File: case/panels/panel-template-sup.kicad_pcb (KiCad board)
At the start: 2 copper layers, 100 x 190 mm, 4 parts

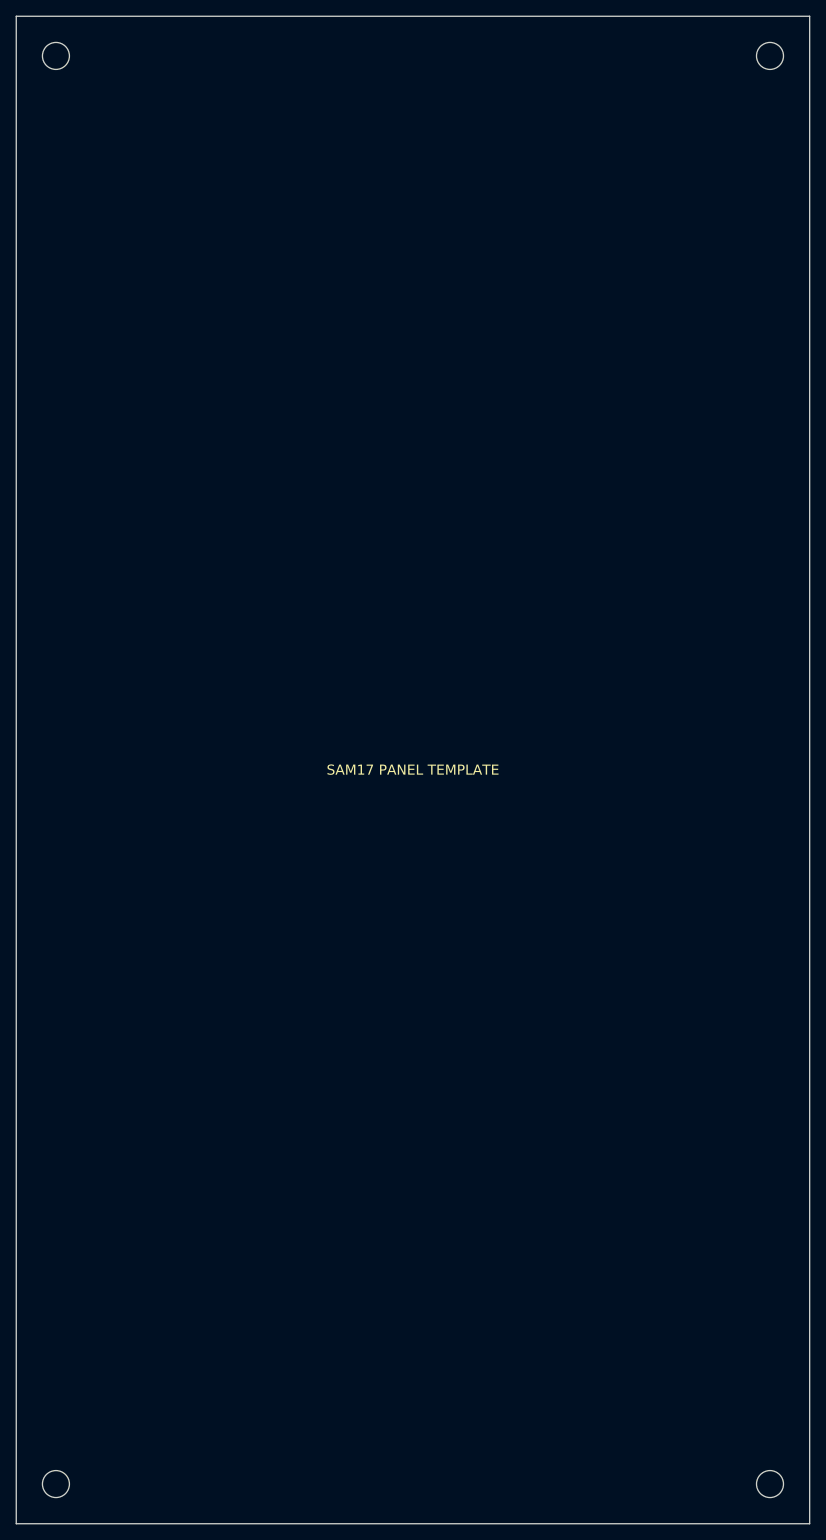
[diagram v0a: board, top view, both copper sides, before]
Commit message: Case: la silueta pasa a triangulo modernista, y tres fallos de raiz que salieron por el camino
La silueta del costado se rehizo entera sobre renders sucesivos. Deja de ser
una bota escalonada y pasa a ser un triangulo rectangulo con la hipotenusa
quebrada en dos tramos y el valle en medio:

  ancho 500   fondo 310.1   alto 269.6
  cara de abajo  55 grados desde la horizontal (35 desde la vertical)
  cara de arriba 45 grados (coincide en las dos convenciones)
  valle 80 mm   marco de remate 22 mm

Cambios de estructura, no solo de cotas:

- prof_superior SE ELIMINA. Eran dos fondos (350 y 250) con una repisa
  escalonada entre ellos, y esa repisa era justo lo que rompia la lectura de
  triangulo. Un solo plano trasero, y una fuente menos de desincronizacion.
  El perfil pasa de 9 puntos a 7: el ANTIGUO P[8] es ahora P[6].

- El FONDO deja de ser parametro y se deriva de marco_remate. Va al reves de
  lo obvio a proposito: con el fondo fijo, cada vez que se movia un angulo o
  un alto de piso el marco cambiaba solo y con el la esquina de arriba. A
  6.7 mm de marco el radio en punta se recorta a 3.3 y la esquina queda casi
  viva; a 57 vuelve la meseta.

- alto_panel se parte en alto_panel_inf / alto_panel_sup. Los dos pisos ya no
  miden lo mismo, asi que la plantilla KiCad se genera por piso
  (--piso inf|sup) y a fichero distinto -- antes las dos escribian el mismo
  nombre y la segunda corrida se comia a la primera en silencio.

- Redondeo POR VERTICE en vez de cierre morfologico global. Un radio unico no
  podia a la vez comerse la cara frontal (que Samuel quiere leyendo como
  punta) y respetar los 80 mm planos del valle. Ahora el valle lleva radios
  OPUESTOS: pico corto en el vertice convexo, radio largo en el concavo.
  Mas entasis (bombeo) en las rectas, excepto el canto de abajo, que es la
  cara de apoyo.

- Fuera el rail "zocalo superior" y la plancha del zocalo: Samuel fijo DOS
  nodos en la esquina de abajo y no tres. 11 largueros -> 10, 5 planchas -> 4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
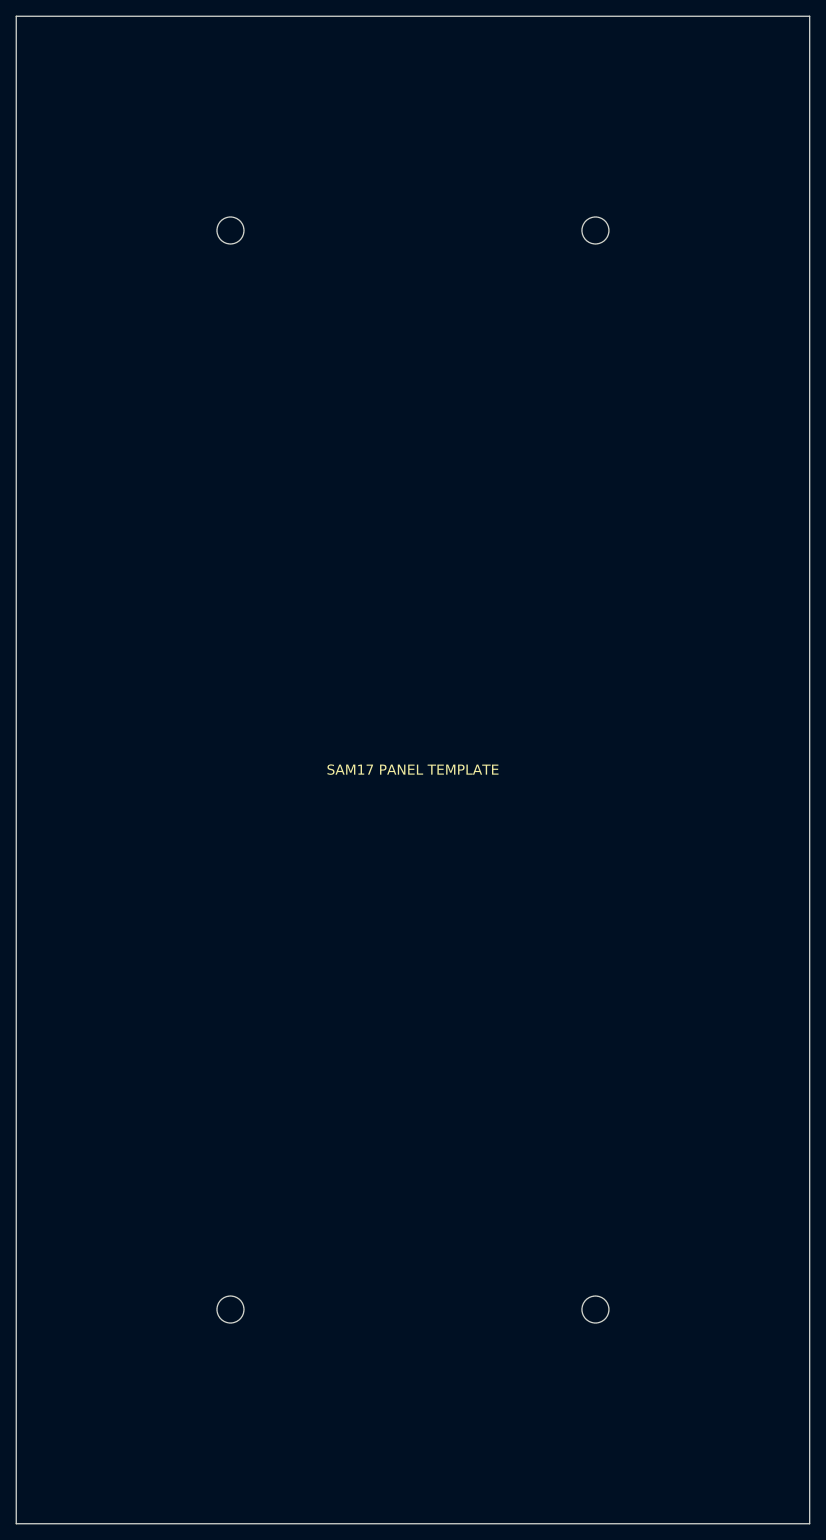
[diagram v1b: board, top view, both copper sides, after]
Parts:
- removed the ? at (95.0, 185.0)
- removed the ? at (95.0, 5.00)
- removed the ? at (5.00, 5.00)
- removed the ? at (5.00, 185.0)
- added ?: , , F.Cu at (27.0, 163.0)
- added ?: , , F.Cu at (73.0, 163.0)
- added ?: , , F.Cu at (27.0, 27.0)
- added ?: , , F.Cu at (73.0, 27.0)
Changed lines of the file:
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@@
 	(footprint ""
 		(layer "F.Cu")
-		(at 95 185)
+		(at 27 163)
 		(property "Reference" ""
 			(at 0 0 0)
@@
 	(footprint ""
 		(layer "F.Cu")
-		(at 95 5)
+		(at 73 163)
 		(property "Reference" ""
 			(at 0 0 0)
@@
 	(footprint ""
 		(layer "F.Cu")
-		(at 5 5)
+		(at 27 27)
 		(property "Reference" ""
 			(at 0 0 0)
@@
 	(footprint ""
 		(layer "F.Cu")
-		(at 5 185)
+		(at 73 27)
 		(property "Reference" ""
 			(at 0 0 0)

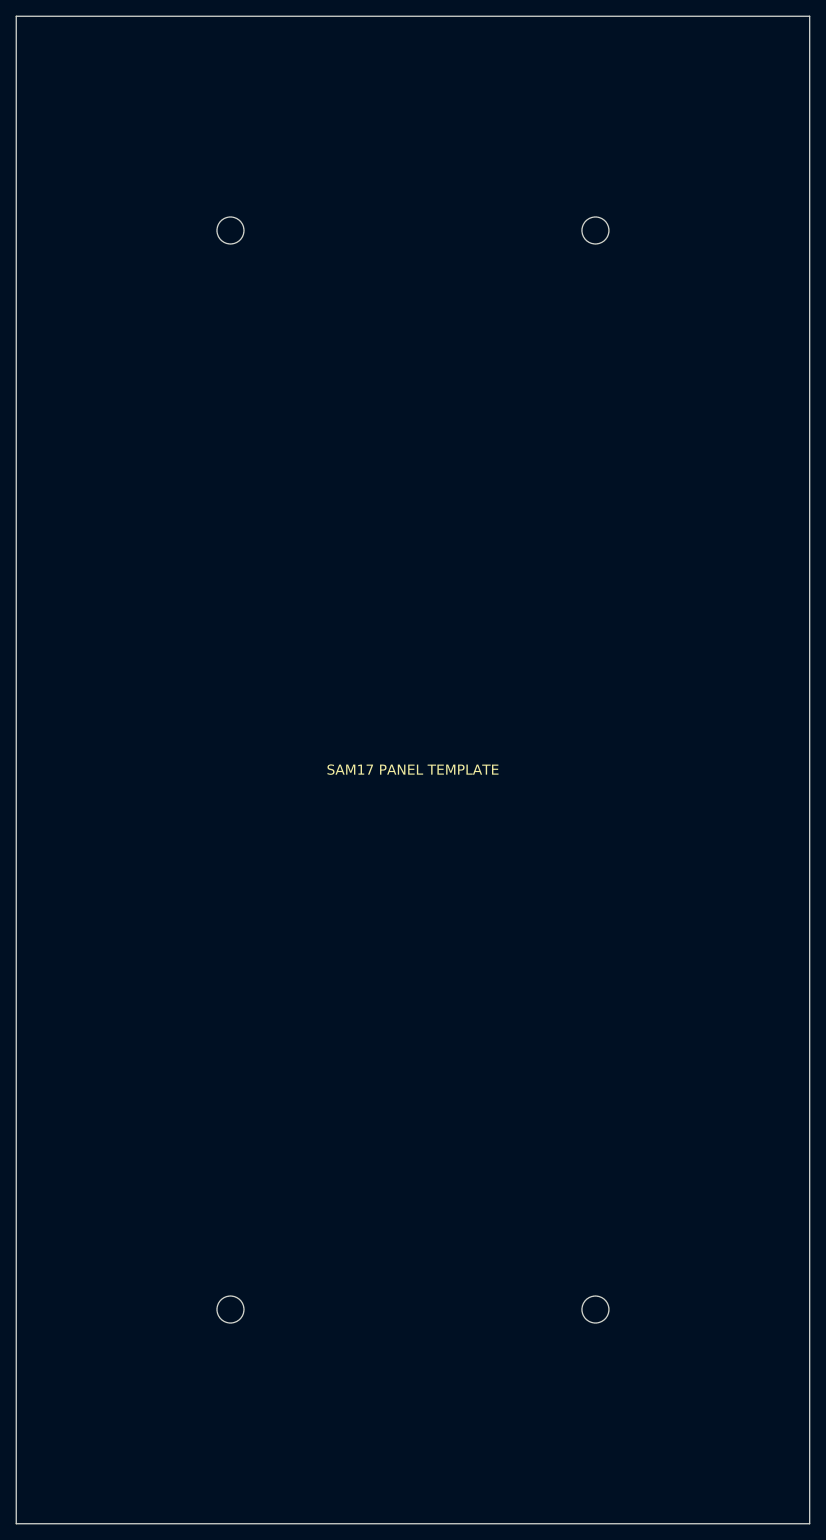
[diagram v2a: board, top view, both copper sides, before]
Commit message: Case: la primera seccion baja al suelo real, que estaba a 2.4 mm
Samuel pidio reducir la primera seccion al maximo que permita EUROrack. Se
midio contra las tres cotas que la limitan en vez de estimarla, y el suelo
resulto estar mucho mas cerca de lo que parecia.

  alto_frontal    30   -> 28
  inset_tornillo  27   -> 26.5
  alto_cara_inf   164.5 -> 164.0   (derivado)
  sep_railes_sup  136  -> 137      (derivado del inset nuevo)

  primera seccion (suelo -> valle)  164.8 -> 162.4
  alto total                        299.1 -> 296.7

Los dos parametros del frente se optimizan JUNTOS, y ese es el nudo: la
altura de la seccion vale alto_frontal + alto_cara_inf*cos(35), y como
alto_cara_inf lleva el inset dentro, la altura ES (alto_frontal +
cos(35)*inset) + una constante. O sea que minimizar el piso es minimizar el
lado izquierdo de la condicion de los dos nodos de la esquina frontal, y esa
condicion tiene suelo.

EL SUELO ES 49.58, NO 44.58, y ahi estuvo el error de la primera pasada: se
derivo contra el lomo del rail de base (y = 20) cuando el techo de verdad es
el TOPE DE LA BANDEJA que se apoya encima de el (y = 25). La bandeja carga el
PSU y va apoyada, no colgada. La version barata daba 8 mm de ganancia y
solapes() la canto en el acto (0.51 mm de solape rail-bandeja). Queda
escrito en params.scad para que nadie vuelva a derivarlo contra el rail.

Con el suelo bueno la ganancia real es 2.4 mm. Los 41.5 mm de acrilico que
envuelven los 122.5 del estandar se reparten asi:

  20.0  medio perfil 2020 a cada punta
  16.6  las dos curvas del contorno (14 la punta del frente, 2.6 el pico)
   4.9  material minimo contra cada curva

La partida grande es la primera y no se toca desde aqui: con un riel EUROrack
de 10 mm en vez de nuestro 2020 la cara baja a ~151 y la seccion pierde 14 mm
-- casi seis veces lo que se gana apretando el acrilico. Eso esta en el correo
a Tobias, no en params.scad.

Puertas: clearance_budget VERDE, check_dxf VERDE (10 largueros dentro del
contorno 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
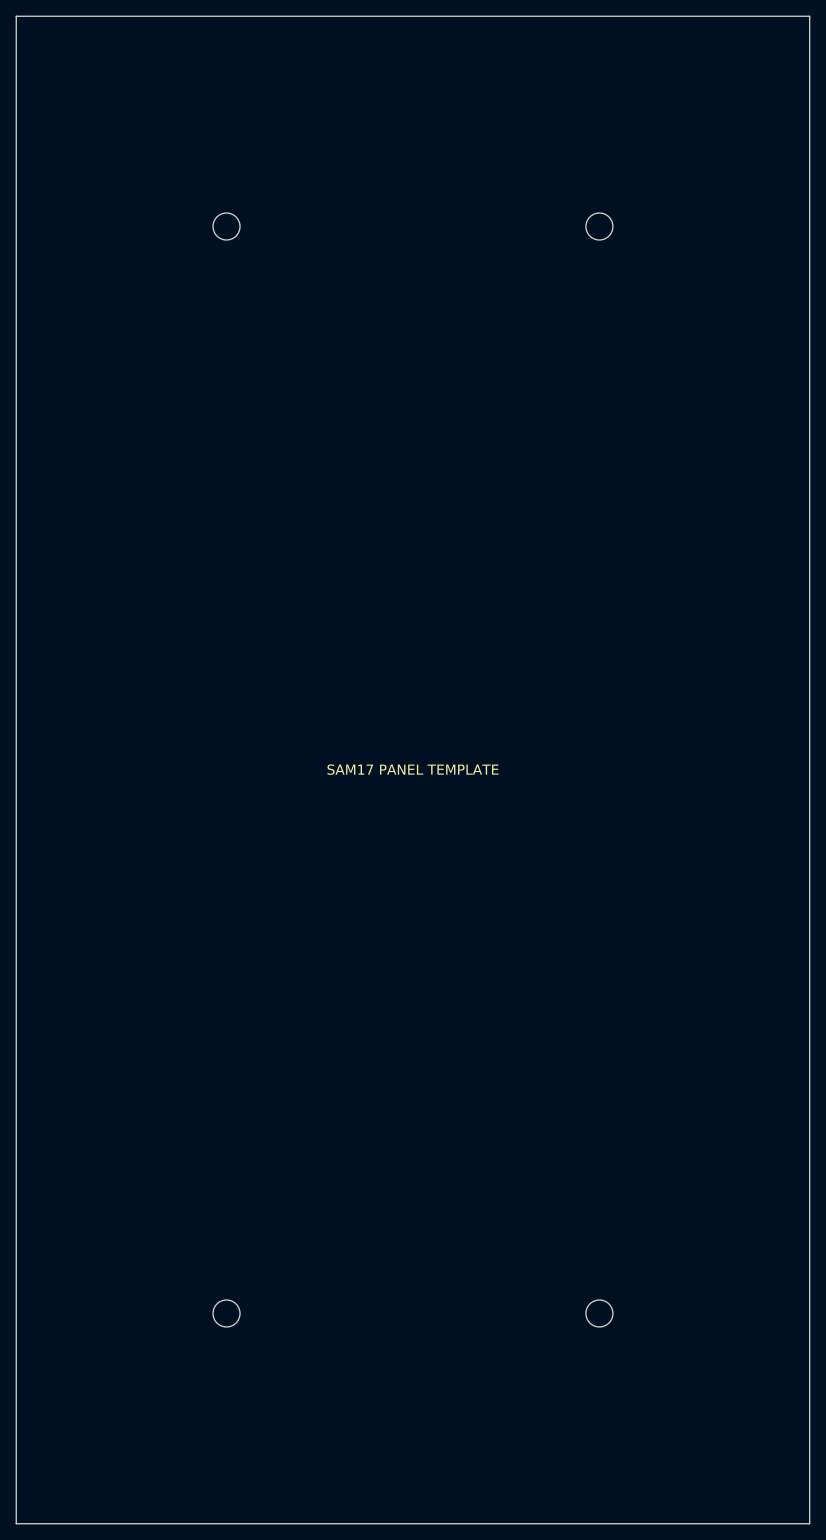
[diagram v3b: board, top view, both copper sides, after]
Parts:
- removed the ? at (73.0, 163.0)
- removed the ? at (27.0, 27.0)
- removed the ? at (73.0, 27.0)
- removed the ? at (27.0, 163.0)
- added ?: , , F.Cu at (73.5, 26.5)
- added ?: , , F.Cu at (26.5, 26.5)
- added ?: , , F.Cu at (73.5, 163.5)
- added ?: , , F.Cu at (26.5, 163.5)
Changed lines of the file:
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@@
 	(footprint ""
 		(layer "F.Cu")
-		(at 73 163)
+		(at 73.5 26.5)
 		(property "Reference" ""
 			(at 0 0 0)
@@
 	(footprint ""
 		(layer "F.Cu")
-		(at 27 27)
+		(at 26.5 26.5)
 		(property "Reference" ""
 			(at 0 0 0)
@@
 	(footprint ""
 		(layer "F.Cu")
-		(at 73 27)
+		(at 73.5 163.5)
 		(property "Reference" ""
 			(at 0 0 0)
@@
 	(footprint ""
 		(layer "F.Cu")
-		(at 27 163)
+		(at 26.5 163.5)
 		(property "Reference" ""
 			(at 0 0 0)
